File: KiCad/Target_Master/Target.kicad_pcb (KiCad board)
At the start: 2 copper layers, 76.2 x 50.8 mm, 44 parts, among them J1 +5V, J2 ICSP, J3 I2C, J4 I2C, J5 I2C, J6 USB_B_Mini, U1 PIC16F1788-IP, U2 FT232RL

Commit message: Master board silkscreen and gerber files
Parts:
- added G***: LOGO, 2025 Logos:Alex_Logo, B.Cu at (172.1, 87.0)
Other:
- board text added: "+5V"
- board text added: "GND"
- board text added: "I2C"
- board text added: "PWR"
- board text added: "RX"
- board text added: "SCL"
- board text added: "SDA"
- board text added: "TX"

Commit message: Target Master Gerbers
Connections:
- C4 pad 1: Net-(C4-Pad1) -> GND
- C5 pad 2: Net-(C5-Pad2) -> GND

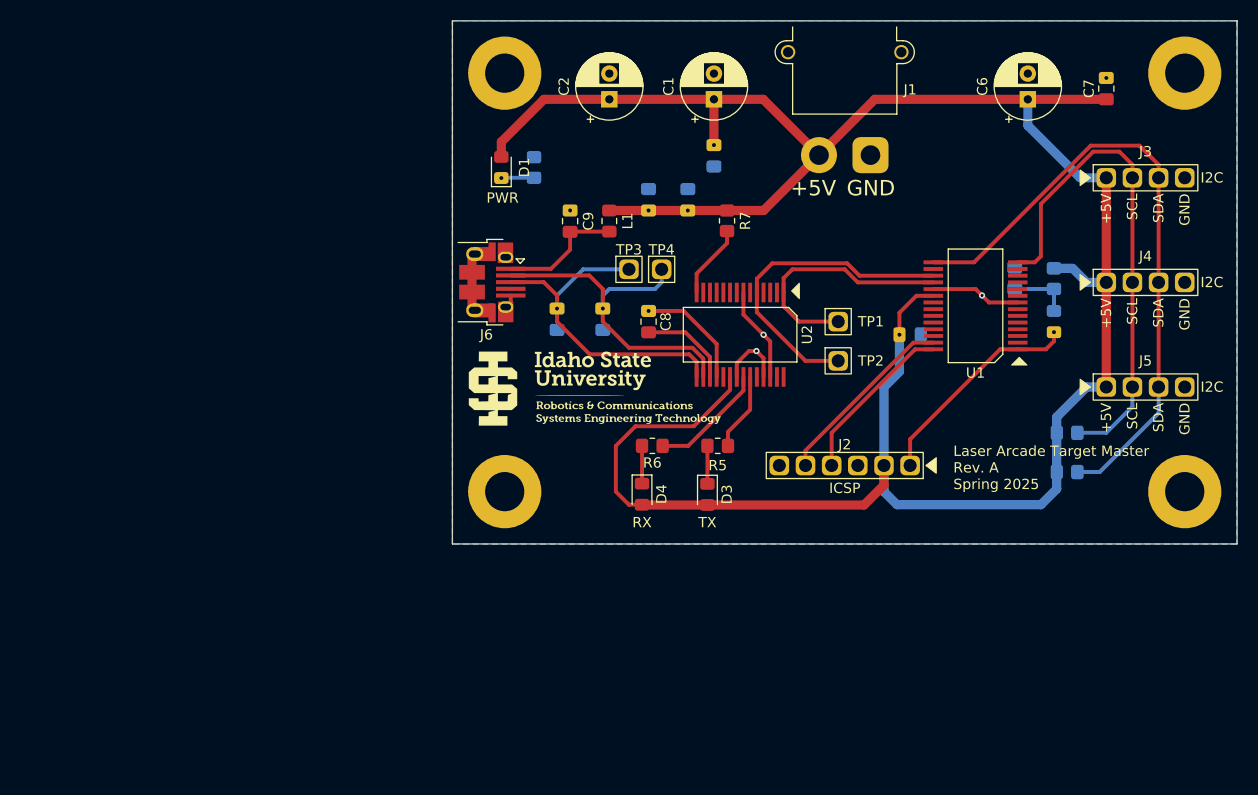
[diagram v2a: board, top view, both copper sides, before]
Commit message: Add titleblock to target PCBs
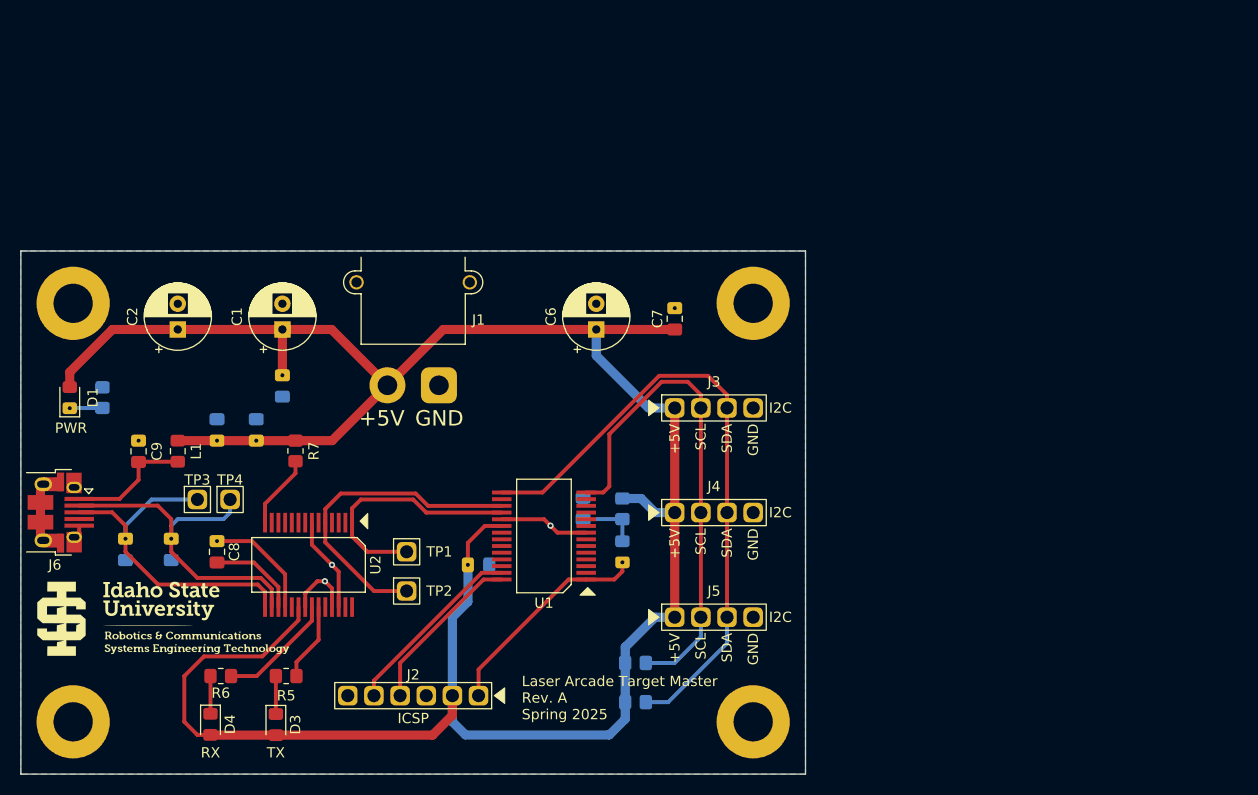
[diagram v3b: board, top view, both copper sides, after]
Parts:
- moved C1 47.5 mm to (135.9, 80.8)
- moved C3 47.5 mm to (135.9, 86.3)
- moved C9 47.5 mm to (121.9, 92.6)
- moved G*** 47.5 mm to (124.5, 108.7)
- moved G*** 47.5 mm to (120.0, 110.6)
- moved D1 47.5 mm to (115.2, 87.4)
- moved ? 47.5 mm to (181.6, 118.9)
- moved ? 47.5 mm to (115.6, 118.9)
- moved C10 47.5 mm to (125.1, 102.1)
- moved C11 47.5 mm to (120.7, 102.1)
- moved C12 47.5 mm to (129.5, 90.5)
- moved C13 47.5 mm to (133.3, 90.5)
- moved C4 47.5 mm to (154.9, 103.6)
- moved C5 47.5 mm to (165.1, 98.1)
- moved C6 47.5 mm to (166.4, 80.8)
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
